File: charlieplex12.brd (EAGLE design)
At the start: 160 x 100 mm, 17 parts

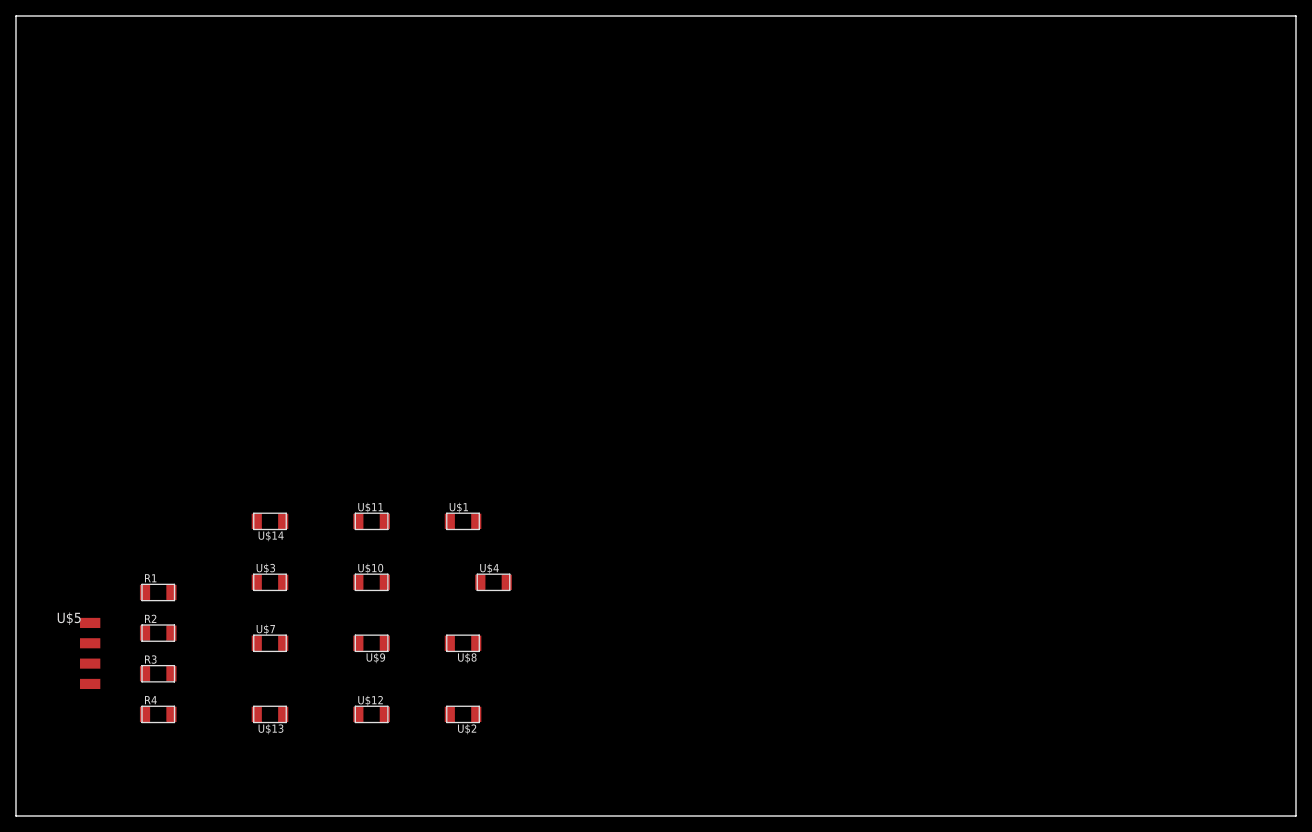
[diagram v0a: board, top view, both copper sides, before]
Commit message: finishing charlieplex layout
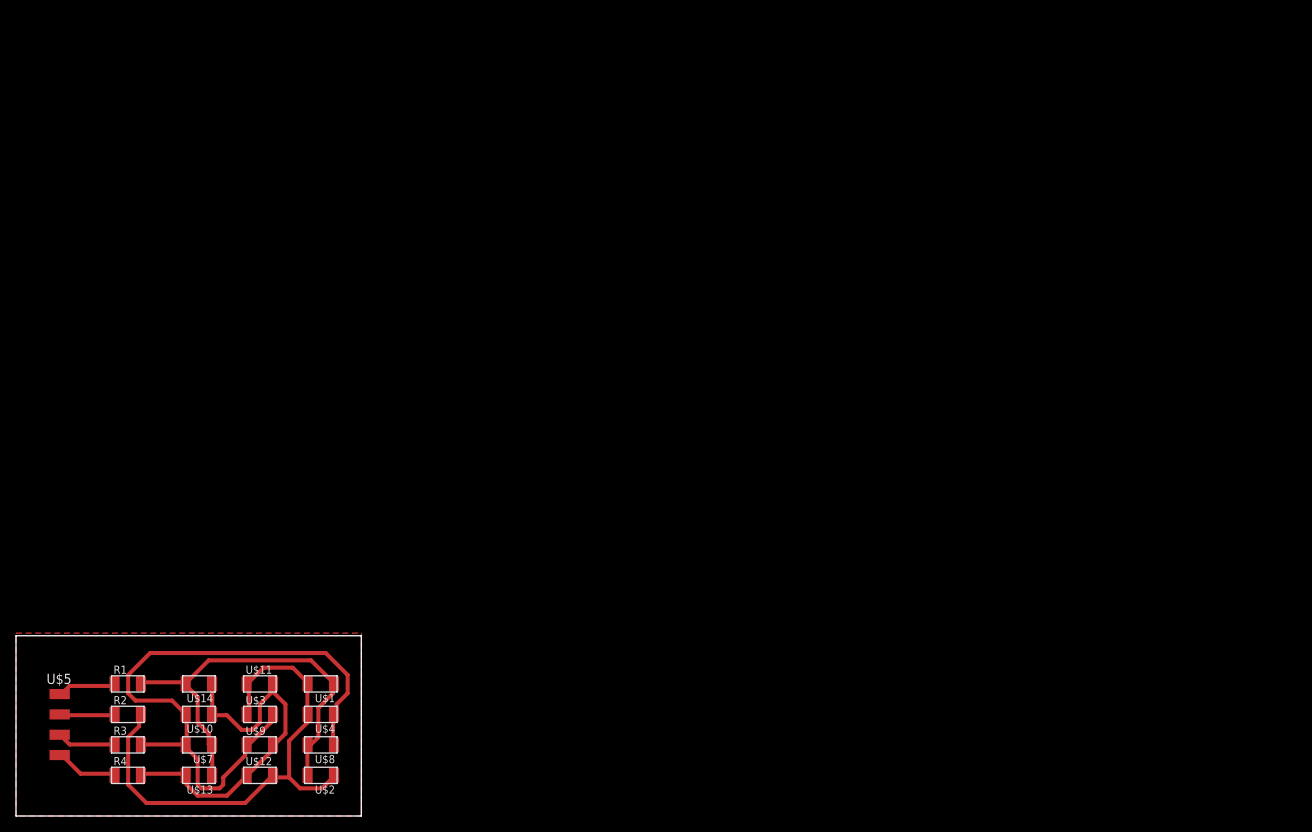
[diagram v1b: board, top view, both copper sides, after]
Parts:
- moved U$10 27.2 mm to (22.9, 12.7), turned to 180 degrees
- moved U$4 27.2 mm to (38.1, 12.7), turned to 180 degrees
- moved U$1 27.0 mm to (38.1, 16.5), turned to 180 degrees
- moved U$11 24.7 mm to (30.5, 16.5)
- moved U$14 22.2 mm to (22.9, 16.5)
- moved U$8 21.8 mm to (38.1, 8.89)
- moved U$2 19.3 mm to (38.1, 5.08)
- moved U$9 18.9 mm to (30.5, 8.89), turned to 0 degrees
- moved U$3 16.6 mm to (30.5, 12.7)
- moved U$12 15.9 mm to (30.5, 5.08)
- moved U$7 15.5 mm to (22.9, 8.89), turned to 180 degrees
- moved R1 12.0 mm to (14.0, 16.5)
- moved U$13 11.7 mm to (22.9, 5.08)
- moved R2 10.9 mm to (14.0, 12.7)
- moved R3 9.67 mm to (14.0, 8.89)
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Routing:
- net N$3: track 0.00 -> 80.1 mm
- net N$2: track 0.00 -> 65.1 mm
- net N$1: track 0.00 -> 52.7 mm
- net N$4: track 0.00 -> 46.9 mm
- net N$8: track 0.00 -> 7.92 mm
- net N$5: track 0.00 -> 7.41 mm
- net N$7: track 0.00 -> 7.37 mm
- net N$6: track 0.00 -> 6.91 mm
- added copper zone on layer 1, net N$9
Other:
- board size 160 x 100 mm -> 43.2 x 22.5 mm
